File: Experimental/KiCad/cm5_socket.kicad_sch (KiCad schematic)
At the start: 24 parts, among them Q1 2N7002, X1 1-2199230-6

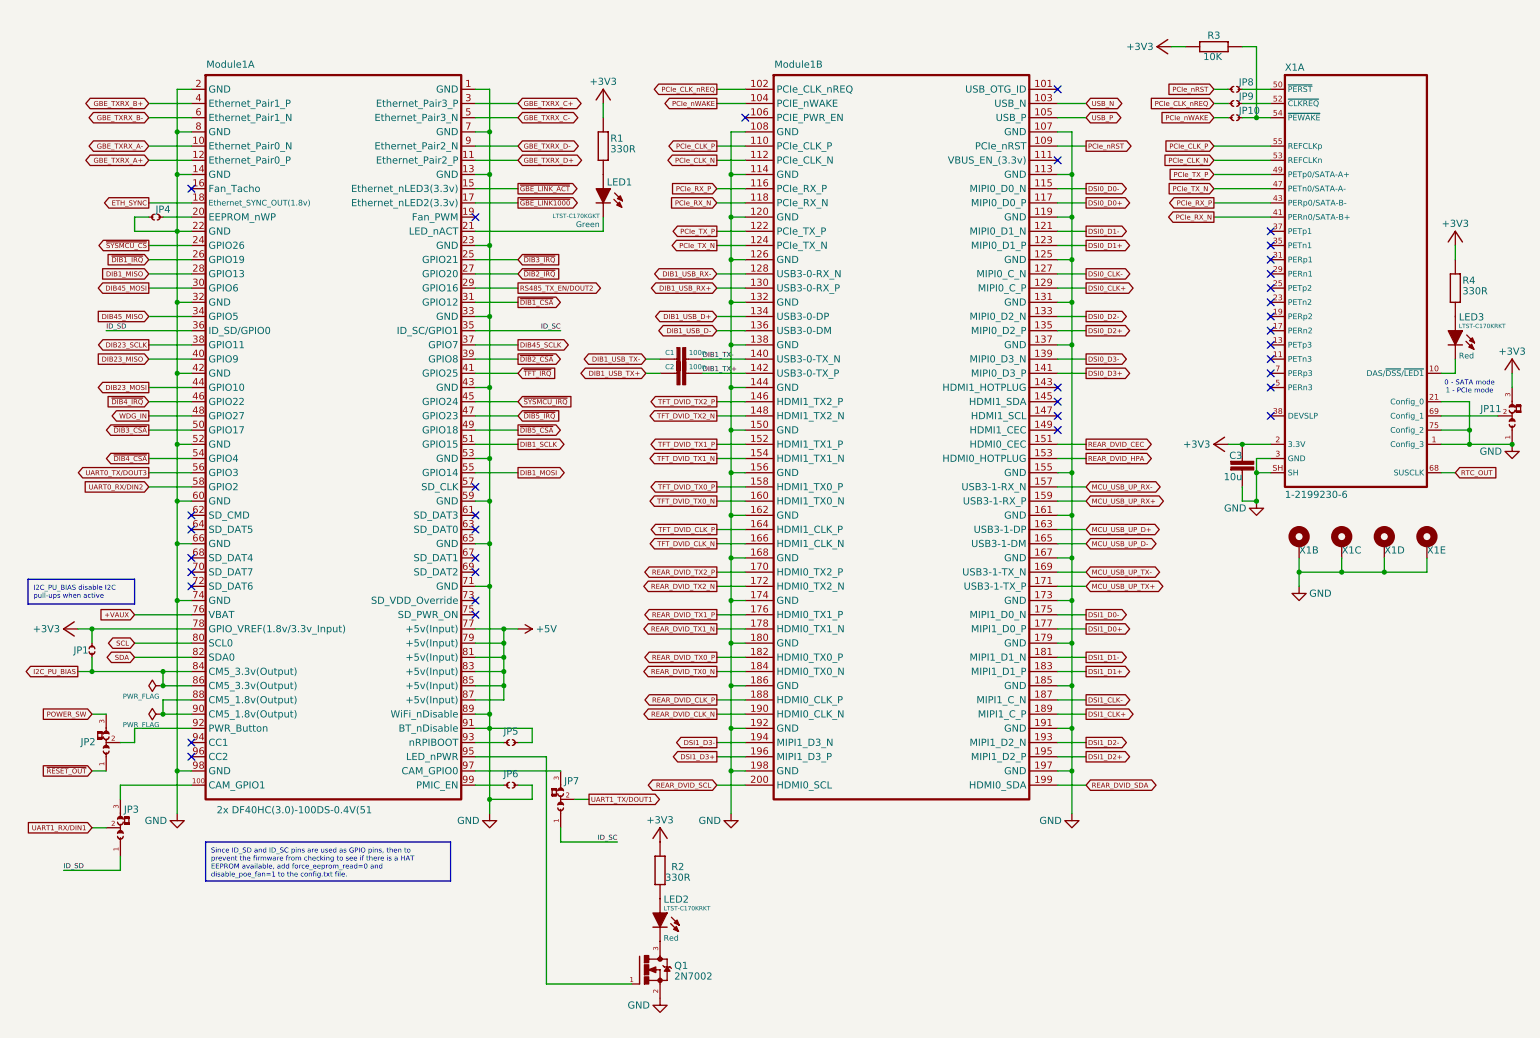
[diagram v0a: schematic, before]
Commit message: Replace 3V3 jumper for H7 CM5 with PMOS sw
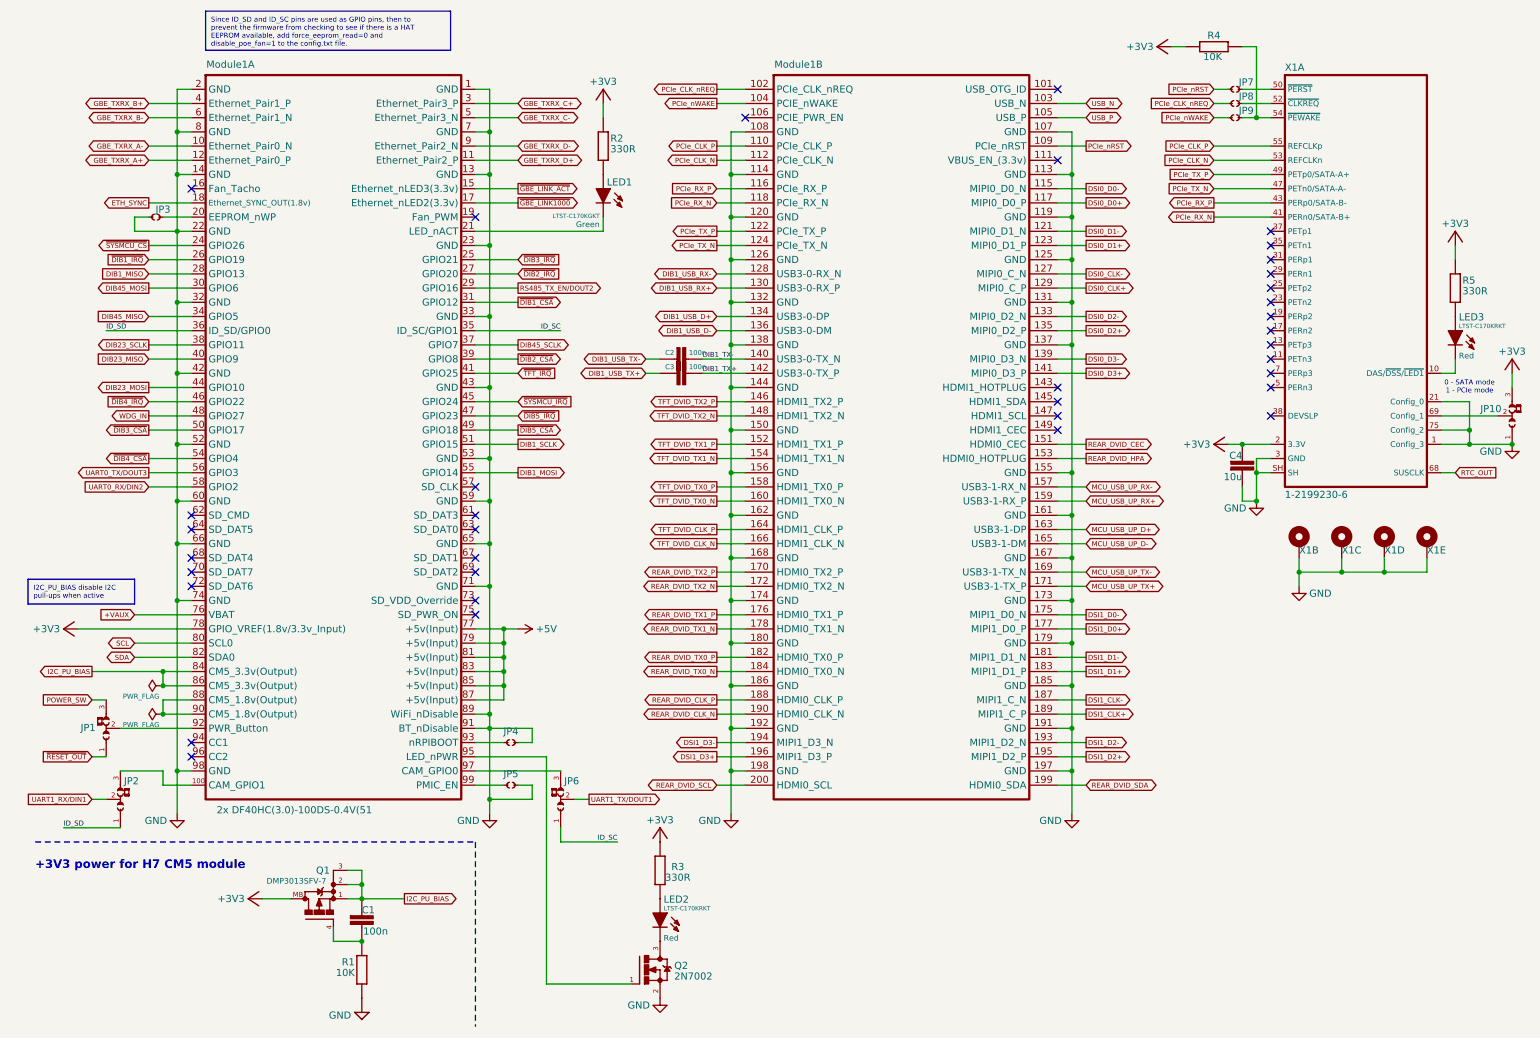
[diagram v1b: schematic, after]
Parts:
- removed JP1: ~, PCM_EEZ_connectors:M22-2010246, symbol PCM_EEZ_unsorted:JP2 open
- added C1: 100n, PCM_EEZ_passives:C_0603_1608Metric, symbol PCM_EEZ_passives:C-EU
- added Q1: DMP3013SFV-7, PCM_EEZ_SMD:TRANS_FDMC8010, symbol PCM_EEZ_discretes:PMOS_LFPAK
- added R1: 10K, PCM_EEZ_passives:R_0603_1608Metric, symbol PCM_EEZ_passives:R-EU
- renumbered C1 to C2, C2 to C3, C3 to C4, JP2 to JP1, JP11 to JP10, JP3 to JP2, JP4 to JP3, JP5 to JP4, JP6 to JP5, JP7 to JP6, JP8 to JP7, JP9 to JP8, JP10 to JP9, Q1 to Q2, R1 to R2, R2 to R3, R3 to R4, R4 to R5
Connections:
- net +3V3: now also Q1.MB
- net GND: now also R1.2
- net I2C_PU_BIAS: now also C1.2, Q1.1 (S), Q1.2 (S), Q1.3 (S)
- new net: C1.1, Q1.4 (G), R1.1
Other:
- note added: "+3V3 power for H7 CM5 module"
- moved on the sheet: JP1, JP2

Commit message: Jumpers update
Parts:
- JP1: symbol PCM_EEZ_unsorted:JP3 shorted with 0R (2-3) -> PCM_EEZ_unsorted:JP3 2mm THT (2-3)
- JP2, JP6: value ~ -> 0R; now in the parts list
- JP3, JP4, JP5: symbol PCM_EEZ_unsorted:JP2 open -> PCM_EEZ_unsorted:JP2 open 2mm THT; DigiKey (none) -> M22-2010346-ND; LCSC (none) -> C5790018; Mouser (none) -> 855-M22-2010246; TME (none) -> -; now in the parts list
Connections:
- net TFT_DVID_HPA: now reaches Module1.143 (HDMI1_HOTPLUG)
- net TFT_DVID_SDA: now reaches Module1.145 (HDMI1_SDA)
- net TFT_DVID_SCL: now reaches Module1.147 (HDMI1_SCL)
- net TFT_DVID_CEC: now reaches Module1.149 (HDMI1_CEC)
- net I2C_PU_BIAS renamed CM5_3V3
- no-connect marks 36 -> 32

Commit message: Power switch modified
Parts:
- JP3, JP4, JP5: DigiKey M22-2010346-ND -> 952-3309-ND
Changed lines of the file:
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@@
 	(title_block
 		(title "${project_name}")
-		(date "2025-10-21")
+		(date "2025-10-23")
 		(rev "${project_version}")
 		(company "${project_creator}")
@@
 			)
 		)
-		(property "DigiKey" "M22-2010346-ND"
+		(property "DigiKey" "952-3309-ND"
 			(at 38.1 55.88 0)
 			(show_name yes)
@@
 			)
 		)
-		(property "DigiKey" "M22-2010346-ND"
+		(property "DigiKey" "952-3309-ND"
 			(at 99.06 157.48 0)
 			(show_name yes)
@@
 			)
 		)
-		(property "DigiKey" "M22-2010346-ND"
+		(property "DigiKey" "952-3309-ND"
 			(at 99.06 149.86 0)
 			(show_name yes)

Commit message: BOM update
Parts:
- Module1: value 2x DF40HC(3.0)-100DS-0.4V(51 -> 2x 10164227-1004A1RLF; DigiKey 26-DF40HC(3.0)-100DS-0.4V(51)CT-ND -> 609-10164227-1004A1RLFCT-ND; LCSC C424649 -> C7435219; Mouser 798-DF40HC30100DS451 -> 649-101642271004RLF
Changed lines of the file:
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@@
 	(title_block
 		(title "${project_name}")
-		(date "2025-10-23")
+		(date "2025-10-25")
 		(rev "${project_version}")
 		(company "${project_creator}")
@@
 			)
 		)
-		(property "Value" "2x DF40HC(3.0)-100DS-0.4V(51"
+		(property "Value" "2x 10164227-1004A1RLF"
 			(at 61.595 156.845 0)
 			(effects
@@
 			)
 		)
-		(property "DigiKey" "26-DF40HC(3.0)-100DS-0.4V(51)CT-ND"
+		(property "DigiKey" "609-10164227-1004A1RLFCT-ND"
 			(at 45.72 25.4 0)
 			(effects
@@
 			)
 		)
-		(property "Mouser" "798-DF40HC30100DS451 "
+		(property "Mouser" "649-101642271004RLF"
 			(at 45.72 25.4 0)
 			(effects
@@
 			)
 		)
-		(property "LCSC" "C424649"
+		(property "LCSC" "C7435219"
 			(at 45.72 25.4 0)
 			(effects
@@
 			)
 		)
-		(property "Value" "2x DF40HC(3.0)-100DS-0.4V(51"
+		(property "Value" "2x 10164227-1004A1RLF"
 			(at 170.18 22.86 0)
 			(effects
@@
 			)
 		)
-		(property "DigiKey" "26-DF40HC(3.0)-100DS-0.4V(51)CT-ND"
+		(property "DigiKey" "609-10164227-1004A1RLFCT-ND"
 			(at 147.32 25.4 0)
 			(effects
@@
 			)
 		)
-		(property "Mouser" "798-DF40HC30100DS451 "
+		(property "Mouser" "649-101642271004RLF"
 			(at 147.32 25.4 0)
 			(effects
@@
 			)
 		)
-		(property "LCSC" "C424649"
+		(property "LCSC" "C7435219"
 			(at 147.32 25.4 0)
 			(effects
